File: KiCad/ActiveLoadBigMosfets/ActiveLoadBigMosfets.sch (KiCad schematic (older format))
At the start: 106 parts

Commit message: More PCB work
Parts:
- removed C? (x3): 10u/X7R/100V, symbol Device:C
- removed C?: 10u, symbol Device:C
- removed J?: FanOut, symbol Connector_Generic:Conn_01x03
- removed Q?: IRLML2244, Package_TO_SOT_SMD:SOT-23, symbol Transistor_FET:IRLML5203
- removed SW?: Rotary_Encoder_Switch, symbol Device:Rotary_Encoder_Switch
- removed U? (x3): TLV2372, symbol Amplifier_Operational:TLV2372
- added C13: 63SXV33M, Capacitor_SMD:CP_Elec_8x11.9, symbol Device:CP
- added C14: 4u7/16V/85mR, Capacitor_SMD:C_0805_2012Metric, symbol Device:C
- added C15: 10n, Capacitor_SMD:C_0805_2012Metric, symbol Device:C
- added C22, C48: 6TPE150MF, Capacitor_Tantalum_SMD:CP_EIA-7343-31_Kemet-D, symbol Device:CP
- added C31, C33, C35: 10u, Capacitor_SMD:C_0805_2012Metric, symbol Device:C
- added C34, C36, C49: 100n, Capacitor_SMD:C_0805_2012Metric, symbol Device:C
- added C40, C41, C42, C43, C44: 1n, Capacitor_SMD:C_0805_2012Metric, symbol Device:C
- added C50: 10u/10V, Capacitor_SMD:C_0805_2012Metric, symbol Device:C
- added F1: 10A, JPFuses:Fuseholder5x20_horiz_open_inline_Type-I, symbol Device:Fuse
- added FL1, FL2: BNX025, Filter:Filter_Murata_BNX025, symbol Filter:BNX025
- added H1, H2, H3, H4: MountingHole, MountingHole:MountingHole_3.2mm_M3, symbol Mechanical:MountingHole
- added J6: FanOut, Connector:FanPinHeader_1x04_P2.54mm_Vertical, symbol Connector_Generic:Conn_01x04
- added J7: PowerInput2, JPConnectors:SolderingHoles-2_P6.00mm_D2.0mm, symbol Connector_Generic:Conn_01x02
- added J8: PowerInput3, JPConnectors:SolderingHoles-2_P6.00mm_D2.0mm, symbol Connector_Generic:Conn_01x02
- added J9: PowerInput4, JPConnectors:SolderingHoles-2_P6.00mm_D2.0mm, symbol Connector_Generic:Conn_01x02
- added Q1: IRLML2502, Package_TO_SOT_SMD:SOT-23, symbol Transistor_FET:IRLML2060
- added Q10, Q11, Q12, Q13, Q14: IXFK44N50P, Package_TO_SOT_THT:TO-264-3_Vertical, symbol Device:Q_NMOS_GDS
- added R13: 100k, Resistor_SMD:R_0805_2012Metric, symbol Device:R
- added R27, R28, R29, R30, R32, R39, R40, R41, R42, R44, R64, R65: 10k, Resistor_SMD:R_0805_2012Metric, symbol Device:R
- added R33, R34, R35, R36, R37: 15k, Resistor_SMD:R_0805_2012Metric, symbol Device:R
- added R45, R46, R49, R50, R55: 0R1, Resistor_SMD:R_2512_6332Metric, symbol Device:R
- added R53, R54, R56, R57, R61: 1k, Resistor_SMD:R_0805_2012Metric, symbol Device:R
- added R63: 20m, Resistor_SMD:R_2512_6332Metric, symbol Device:R
- added R66, R67, R68, R69: 10, Resistor_SMD:R_0805_2012Metric, symbol Device:R
- added R70: 5k, Resistor_SMD:R_0805_2012Metric, symbol Device:R
- added RV1: 5k, Potentiometer_SMD:Potentiometer_ACP_CA6-VSMD_Vertical, symbol Device:R_POT
- added SW1: Rotary_Encoder_Switch, Rotary_Encoder:RotaryEncoder_Alps_EC11E-Switch_Vertical_H20mm_CircularMountingHoles, symbol Device:Rotary_Encoder_Switch
- added SW2: SW_Push, Button_Switch_SMD:SW_SPST_EVQP0, symbol Switch:SW_Push
- added U5, U6, U7: TLV2374, Package_SO:SOIC-14_3.9x8.7mm_P1.27mm, symbol myLib:TLV2374
- C1, C10, C16, C17, C18, C19, C2, C20, C21, C23, C24, C25, C26, C3, C30, C32, C37, C38, C39, C4, C45, C46, C47, C5, C6, C7, C8, C9: renamed from C?; footprint (none) -> Capacitor_SMD:C_0805_2012Metric
- C11, C12: renamed from C?; footprint (none) -> Capacitor_Tantalum_SMD:CP_EIA-7343-31_Kemet-D
- C27, C28: renamed from C?; value 10u/16V/85mR -> 4u7/16V/85mR; footprint (none) -> Capacitor_SMD:C_0805_2012Metric
- C29: renamed from C?; footprint (none) -> Capacitor_SMD:CP_Elec_6.3x7.7
- D1, D2: renamed from D?; footprint (none) -> Diode_SMD:D_SMB
- D3: renamed from D?; footprint (none) -> Diode_SMD:D_MiniMELF
- D4: renamed from D?; footprint (none) -> LED_SMD:LED_0805_2012Metric
- J1: renamed from J?; footprint (none) -> Connector_FFC-FPC:TE_0-1734839-6_1x06-1MP_P0.5mm_Horizontal
- J2: renamed from J?; footprint (none) -> JPConnectors:SolderingHoles-2_P6.00mm_D2.0mm
- J3: renamed from J?; footprint (none) -> Connector_PinHeader_2.54mm:PinHeader_1x06_P2.54mm_Vertical
- J4: renamed from J?; footprint (none) -> JPConnectors:Hirose_FH12-50S-0.5SH_1x50-1MP_P0.50mm_Horizontal
- J5: renamed from J?; footprint (none) -> Connector_PinHeader_2.54mm:PinHeader_2x10_P2.54mm_Vertical_SMD
- L1: renamed from L?; footprint (none) -> Inductor_SMD:L_0805_2012Metric
- L2: renamed from L?; footprint (none) -> JPInductors:L_Wuerth_WE-HCF
- L3: renamed from L?; value L -> 7447714330; footprint (none) -> Inductor_SMD:L_Wuerth_WE-PDF
- Q9: renamed from Q?; footprint (none) -> Package_TO_SOT_THT:TO-264-3_Vertical
- R1: renamed from R?; value R -> 20m; footprint (none) -> Resistor_SMD:R_2512_6332Metric
- R10, R12, R15, R16, R17, R18, R19, R2, R20, R21, R22, R24, R26, R38, R47, R48, R51, R52, R58, R59, R60, R62, R7, R8: renamed from R?; footprint (none) -> Resistor_SMD:R_0805_2012Metric
- R11: renamed from R?; value 133k -> 30k; footprint (none) -> Resistor_SMD:R_0805_2012Metric
- R14: renamed from R?; value 10k2 -> 15k4; footprint (none) -> Resistor_SMD:R_0805_2012Metric
- R23: renamed from R?; value 86k6 -> 100k; footprint (none) -> Resistor_SMD:R_0805_2012Metric
- R25: renamed from R?; value 10k -> 11k; footprint (none) -> Resistor_SMD:R_0805_2012Metric
- R3, R6: renamed from R?; footprint (none) -> Jumper:SolderJumper-2_P1.3mm_Bridged_RoundedPad1.0x1.5mm
- R31: renamed from R?; value 10k -> 15k; footprint (none) -> Resistor_SMD:R_0805_2012Metric
- R4, R5: renamed from R?; footprint (none) -> Jumper:SolderJumper-2_P1.3mm_Open_RoundedPad1.0x1.5mm
- R43: renamed from R?; footprint (none) -> Resistor_SMD:R_2512_6332Metric
- R9: renamed from R?; value 44k2 -> 68k; footprint (none) -> Resistor_SMD:R_0805_2012Metric
- U1: renamed from U?; footprint (none) -> Package_SO:SOIC-8-1EP_3.9x4.9mm_P1.27mm_EP2.41x3.3mm_ThermalVias
- U2: renamed from U?; footprint (none) -> Package_TO_SOT_SMD:SOT-223-3_TabPin2
- U4: renamed from U?; value LM2735XMF -> LM2735YMF
- U8: renamed from U?; footprint (none) -> Package_TO_SOT_THT:TO-220-5_Vertical
- Y1: renamed from Y?; footprint (none) -> Crystal:Crystal_SMD_5032-2Pin_5.0x3.2mm
- gave numbers to parts that had none: 9
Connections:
- net GNDPWR is gone; now on net GND: D1.2 (A), J2.1 (Pin_1), R43.2
- net +12V: now also C31.1, C33.1, C34.1, C35.1, C36.1, FL2.2 (CB), R70.1, U5.4 (V+), U6.4 (V+), U7.4 (V+); no longer C26.1, C27.1, C28.1, C29.1, D2.1 (K), R23.2
- net +3V3: now also C22.1, C49.1, R64.1, R66.2, R67.2, R68.2, R69.2; no longer R2.2
- net +4V: now also C48.1, C50.1, FL1.2 (CB); no longer C10.1, C11.1, C12.1, L2.2, R9.1
- net DisplayLEDCtrl: now also Q1.1 (G)
- net Enc_A: now also U3.22 (PA6); no longer U3.58 (PB6)
- net Enc_B: now also U3.23 (PA7); no longer U3.59 (PB7)
- net Enc_Switch: now also U3.41 (PA8); no longer U3.61 (PB8)
- net FanPWD: now also U3.21 (PA5), J6.4 (Pin_4); no longer Q8.1 (G), U3.22 (PA6)
- net FanSensor: now also U3.27 (PB1), J6.3 (Pin_3); no longer U3.23 (PA7)
- net GND: now also U1.7 (GND), U1.9 (PowerPAD), C13.2, FL1.3 (PSG), J7.1 (Pin_1), J8.1 (Pin_1), J9.1 (Pin_1), R13.2, R45.2, R46.2, R49.2, R50.2, R55.2; no longer C1.2, C17.2, C18.2, C19.2, C2.2, C20.2, C21.2, C23.2, C24.2, C25.1, C27.2, C28.2, C29.2, C3.2, C30.2, C32.2, C37.2, C38.2, C4.2, C45.2, C46.2, C47.2, C5.2, C6.2, C7.1, D3.2 (A), D4.1 (K), J1.6 (Pin_6), J3.3 (Pin_3), J4.1 (Pin_1), J4.11 (Pin_11), J4.12 (Pin_12), J4.13 (Pin_13), J4.14 (Pin_14), J4.34 (Pin_34), J4.43 (Pin_43), J4.48 (Pin_48), J4.49 (Pin_49), J4.50 (Pin_50), J4.8 (Pin_8), J4.9 (Pin_9), J5.10 (Pin_10), J5.12 (Pin_12), J5.14 (Pin_14), J5.16 (Pin_16), J5.18 (Pin_18), J5.20 (Pin_20), J5.4 (Pin_4), J5.6 (Pin_6), J5.8 (Pin_8), Q4.2 (S), Q5.2 (S), Q6.2 (S), Q7.2 (S), R11.2, R16.2, R17.2, R18.2, R19.2, R21.1, R25.1, R48.2, R5.2, R6.2, U2.2 (GND), U3.12 (VSSA), U3.18 (VSS), U3.31 (VSS), U3.47 (VSS), U3.60 (BOOT0), U3.63 (VSS), U4.2 (GND), U8.3 (GND), U9.1 (A1), U9.2 (A0), U9.7 (GND)
- net LCD_D_C: now also U3.59 (PB7)
- net LCD_RDX: now also U3.57 (PB5)
- net LCD_RESET: now also U3.50 (PA15)
- net LCD_SELECT: now also U3.61 (PB8)
- net LCD_WRX: now also U3.58 (PB6)
- net LED: now also U3.33 (PB12); no longer U3.50 (PA15)
- net LoadLevel: now also RV1.2, U5.10 (+), U5.5 (+), U6.10 (+), U6.5 (+), U7.10 (+), U7.5 (+)
- net PowerIn+: now also F1.1, R63.2; no longer J2.2 (Pin_2)
- net PowerIn-: now also U1.2 (Vin), U1.3 (EN), C13.1, Q10.2 (D), Q11.2 (D), Q12.2 (D), Q13.2 (D), Q14.2 (D), R63.1
- net at C39.2, Q9.1 (G): now also U5.7
- net at C39.1, R26.2: now also U5.6 (-)
- net at R38.2: now also U5.3 (+)
- net at R31.1, R48.1: now also U5.2 (-)
- net at R26.1, R31.2: now also U5.1
- net at D3.1 (K), Q8.2 (S): now also J6.2 (Pin_2)
- net at U1.1 (Boot): now also C8.2
- net at U1.4 (RT_SYNC): now also R11.1
- net at U1.5 (FB): now also C10.2, R14.1, R9.2
- net at U1.6 (SS): now also C16.1
- net at U1.8 (SW): now also C8.1, D1.1 (K), L2.2
- net Switch: now reaches U3.42 (PA9)
- net Switch: now also C15.1, R65.1
- net FanPower: now reaches U3.45 (PA12)
- net FanPower: now also Q8.1 (G)
- net GNDD: now reaches R20.1, R22.1
- net GNDD: now also C1.2, C17.2, C18.2, C19.2, C2.2, C20.2, C21.2, C23.2, C24.2, C25.1, C27.2, C28.2, C29.2, C3.2, C30.2, C37.2, C38.2, C4.2, C45.2, C46.2, C47.2, C5.2, C6.2, C7.1, D4.1 (K), J1.6 (Pin_6), J3.3 (Pin_3), J4.11 (Pin_11), J4.12 (Pin_12), J4.13 (Pin_13), J4.14 (Pin_14), J4.34 (Pin_34), J4.43 (Pin_43), J4.48 (Pin_48), J4.49 (Pin_49), J4.50 (Pin_50), J4.8 (Pin_8), J4.9 (Pin_9), J5.10 (Pin_10), J5.12 (Pin_12), J5.14 (Pin_14), J5.16 (Pin_16), J5.18 (Pin_18), J5.20 (Pin_20), J5.4 (Pin_4), J5.6 (Pin_6), J5.8 (Pin_8), Q4.2 (S), Q5.2 (S), Q6.2 (S), Q7.2 (S), R16.2, R17.2, R18.2, R19.2, R2.2, R21.1, R25.1, R5.2, R6.2, U2.2 (GND), U3.12 (VSSA), U3.18 (VSS), U3.31 (VSS), U3.47 (VSS), U3.60 (BOOT0), U3.63 (VSS), U4.2 (GND), U8.3 (GND), U9.1 (A1), U9.2 (A0), U9.7 (GND), C14.2, C15.2, C22.2, C48.2, C49.2, C50.2, FL1.4 (CG), FL2.3 (PSG), Q1.2 (S), RV1.3, SW1.C, SW1.S2, SW2.1
- net at R52.2, R58.1: now also SW1.B
- net at R51.2, R62.1: now also SW1.A
- net at R47.2, R59.2: now also SW1.S1
- new net: F1.2, J2.2 (Pin_2), J7.2 (Pin_2), J8.2 (Pin_2), J9.2 (Pin_2)
- new net: C14.1, C26.1, C27.1, C28.1, C29.1, D2.1 (K), FL2.1 (B), R23.2
- new net: R11.2, R13.1
- new net: C10.1, C11.1, C12.1, FL1.1 (B), L2.1, R9.1
- new net: J4.1 (Pin_1), Q1.3 (D)
- new net: J4.2 (Pin_2), R66.1
- new net: J4.3 (Pin_3), R67.1
- new net: J4.4 (Pin_4), R68.1
- new net: J4.5 (Pin_5), R69.1
- new net: R70.2, RV1.1
- new net: C40.2, Q10.1 (G), U5.8
- new net: C40.1, R27.2, U5.9 (-)
- new net: R39.2, U5.12 (+)
- new net: R33.1, R53.1, U5.13 (-)
- new net: R27.1, R33.2, U5.14
- new net: Q10.3 (S), R39.1, R45.1
- new net: C41.2, Q11.1 (G), U6.7
- new net: Q11.3 (S), R40.1, R46.1
- new net: R34.1, R54.1, U6.2 (-)
- new net: R40.2, U6.3 (+)
- new net: R28.1, R34.2, U6.1
- new net: C41.1, R28.2, U6.6 (-)
- new net: C42.2, Q12.1 (G), U6.8
- new net: C42.1, R29.2, U6.9 (-)
- new net: R41.2, U6.12 (+)
- new net: R35.1, R56.1, U6.13 (-)
- new net: R29.1, R35.2, U6.14
- new net: Q12.3 (S), R41.1, R49.1
- new net: C43.2, Q13.1 (G), U7.7
- new net: Q13.3 (S), R42.1, R50.1
- new net: R36.1, R57.1, U7.2 (-)
- new net: R42.2, U7.3 (+)
- new net: R30.1, R36.2, U7.1
- new net: C43.1, R30.2, U7.6 (-)
- new net: C44.2, Q14.1 (G), U7.8
- new net: C44.1, R32.2, U7.9 (-)
- new net: R44.2, U7.12 (+)
- new net: R37.1, R61.1, U7.13 (-)
- new net: R32.1, R37.2, U7.14
- new net: Q14.3 (S), R44.1, R55.1
- new net: R64.2, R65.2, SW2.2
- new net GNDA: C31.2, C32.2, C33.2, C34.2, C35.2, C36.2, D3.2 (A), FL2.4 (CG), J6.1 (Pin_1), R48.2, R53.2, R54.2, R56.2, R57.2, R61.2, U5.11 (V-), U6.11 (V-), U7.11 (V-)
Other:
- note added: "G=15"
- note added: "Rthjc=0.2Ohm\nRthcs=1Ohm\nRthsa=0.5Ohm\nRth=1.7Ohm\n(125-40)/1.7=50W\n\nRth=0.25+0+0.5=0.75 Ohm\n85/0.75=114W"
- note added: "Vo=12.665V"
- note added: "Vo=4.062V"
- note added: "https://webench.ti.com/power-designer/switching-regulator/customize/8?AppType=None&Flavor=NA&O1I=1.5&O1V=4&Topology=BUCK&VinMax=30.00&VinMin=5&VoltageOption=NA&base_pn=LMR14020S&flavor=NA&lang_chosen=en_US&op_TA=30&optfactor=3&origin=pf_panel\nhttps://webench.ti.com/power-designer/switching-regulator/customize/7?AppType=None&Flavor=None&O1I=0.4&O1V=12&Topology=Boost&VinMax=4&VinMin=4&VoltageOptio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"
- note removed: "G=10"
- note removed: "Rthjc=0.25Ohm\nRthcs=1Ohm\nRthsa=0.5Ohm\nRth=1.75Ohm\n\n(125-40)/2.25=48W"
- note removed: "https://webench.ti.com/power-designer/switching-regulator/customize/8?AppType=None&Flavor=NA&O1I=1.5&O1V=4&Topology=BUCK&VinMax=30.00&VinMin=5&VoltageOption=NA&base_pn=LMR14020S&flavor=NA&lang_chosen=en_US&op_TA=30&optfactor=3&origin=pf_panel"
- moved on the sheet: C1, C10, C11, C12, C16, C19, C20, C21, C23, C24, C25, C26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

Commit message: More pcb work
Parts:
- added J10: I2C, Connector_PinHeader_2.54mm:PinHeader_1x04_P2.54mm_Vertical, symbol Connector_Generic:Conn_01x04
- C2, C20, C21, C23, C24, C25, C3, C32, C34, C36, C37, C38, C4, C49, C5, C7, C8, C9: footprint Capacitor_SMD:C_0805_2012Metric -> Capacitor_SMD:C_0603_1608Metric
- FL1, FL2: footprint Filter:Filter_Murata_BNX025 -> JPInductors:Filter_Murata_BNX025
- L3: footprint Inductor_SMD:L_Wuerth_WE-PDF -> JPInductors:L_Wuerth_WE-PDF_Handsoldering
- R1, R43, R45, R46, R49, R50, R55, R63: footprint Resistor_SMD:R_2512_6332Metric -> Resistor_SMD:R_2512_6332Metric_Pad1.52x3.35mm_HandSolder
- R10, R12, R20, R21, R22, R24, R26, R27, R28, R29, R30, R32, R38, R39, R40, R41, R42, R44, R47, R51, R52, R58, R59, R60, R62, R64, R65: footprint Resistor_SMD:R_0805_2012Metric -> Resistor_SMD:R_0603_1608Metric
- U4: footprint Package_TO_SOT_SMD:SOT-23-5 -> Package_TO_SOT_SMD:SOT-23-5_HandSoldering
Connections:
- net +3V3: now also J10.1 (Pin_1)
- net GNDD: now also J10.2 (Pin_2)
- net SCL: now also J10.3 (Pin_3)
- net SDA: now also J10.4 (Pin_4)

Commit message: PCB work
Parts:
- J4: footprint JPConnectors:Hirose_FH12-50S-0.5SH_1x50-1MP_P0.50mm_Horizontal -> JPConnectors:Molex-50S-0.5SH_1x50-P0.50mm_Horizontal
- SW2: footprint Button_Switch_SMD:SW_SPST_EVQP0 -> Button_Switch_SMD:SW_SPST_B3S-1000
- U8: footprint Package_TO_SOT_THT:TO-220-5_Vertical -> Connector_PinHeader_2.54mm:PinHeader_1x05_P2.54mm_Vertical
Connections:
- net LCD_RESET: now also U3.49 (PA14); no longer U3.50 (PA15)
- net SCL: now also U8.4 (SCLK); no longer U8.2 (SDA)
- net SDA: now also U8.2 (SDA); no longer U8.4 (SCLK)
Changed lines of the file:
@@
 F 0 "U8" H 4823 8038 40  0000 R CNN
 F 1 "TC74" H 4823 7962 40  0000 R CNN
-F 2 "Package_TO_SOT_THT:TO-220-5_Vertical" H 4950 8000 60  0001 C CNN
+F 2 "Connector_PinHeader_2.54mm:PinHeader_1x05_P2.54mm_Vertical" H 4950 8000 60  0001 C CNN
 F 3 "" H 4950 8000 60  0000 C CNN
 	1    4950 8000
@@
 	1    0    0    -1
 $EndComp
-Text GLabel 5400 7950 2    50   Input ~ 0
+Text GLabel 5400 8050 2    50   Input ~ 0
 SCL
 Text GLabel 6250 2300 2    50   Input ~ 0
 SCL
-Text GLabel 5400 8050 2    50   Input ~ 0
+Text GLabel 5400 7950 2    50   Input ~ 0
 SDA
 Wire Wire Line
@@
 F 0 "J4" H 12850 4067 50  0000 C CNN
 F 1 "RVT28AETNWC00" H 12850 3976 50  0000 C CNN
-F 2 "JPConnectors:Hirose_FH12-50S-0.5SH_1x50-1MP_P0.50mm_Horizontal" H 12800 2650 50  0001 C CNN
+F 2 "JPConnectors:Molex-50S-0.5SH_1x50-P0.50mm_Horizontal" H 12800 2650 50  0001 C CNN
 F 3 "~" H 12800 2650 50  0001 C CNN
 	1    12800 2650
@@
 Wire Wire Line
 	1000 6000 1000 6150
-Text Label 9850 4300 0    50   ~ 0
+Text Label 9850 4200 0    50   ~ 0
 LCD_RESET
 Wire Wire Line
@@
 F 0 "SW2" H 1700 12285 50  0000 C CNN
 F 1 "SW_Push" H 1700 12194 50  0000 C CNN
-F 2 "Button_Switch_SMD:SW_SPST_EVQP0" H 1700 12200 50  0001 C CNN
+F 2 "Button_Switch_SMD:SW_SPST_B3S-1000" H 1700 12200 50  0001 C CNN
 F 3 "~" H 1700 12200 50  0001 C CNN
 	1    1700 12000

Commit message: Latest PCB changes. STM32 Project
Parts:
- removed Y1: Crystal, Crystal:Crystal_SMD_5032-2Pin_5.0x3.2mm, symbol Device:Crystal
- added Q15, Q16: IRLML2244, Package_TO_SOT_SMD:SOT-23, symbol Transistor_FET:IRLML5203
- added Q17: IRLML2502, Package_TO_SOT_SMD:SOT-23, symbol Transistor_FET:IRLML2060
- added R71, R72: 100k, Resistor_SMD:R_0805_2012Metric, symbol Device:R
- added TP1, TP10, TP11, TP12, TP2, TP3, TP4, TP5, TP6, TP7, TP8, TP9: TestPoint, TestPoint:TestPoint_THTPad_1.5x1.5mm_Drill0.7mm, symbol Connector:TestPoint
- added Y1: 16MHz, Crystal:Crystal_SMD_Abracon_ABM3B-4Pin_5.0x3.2mm, symbol Device:Crystal_GND24
- R60: value 10k -> 4k7; footprint Resistor_SMD:R_0603_1608Metric -> Resistor_SMD:R_0805_2012Metric
- R7, R8: value 2k2 -> 4k7
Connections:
- net +12V: now also Q15.2 (S), Q16.2 (S), R71.2, R72.2, TP6.1; no longer C31.1, C32.1, C33.1, C34.1, C35.1, C36.1, Q8.3 (D), U5.4 (V+), U6.4 (V+), U7.4 (V+)
- net +3V3: now also TP11.1
- net +4V: now also TP2.1
- net DisplayLEDCtrl: now also U3.45 (PA12); no longer U3.46 (PA13)
- net FanSensor: now also U3.62 (PB9); no longer U3.27 (PB1)
- net GND: now also TP3.1
- net GNDA: now also C33.1, Q8.2 (S), Q17.2 (S), TP8.1; no longer C33.2
- net GNDD: now also TP10.1, TP12.1, TP4.1, TP7.1, Y1.2, Y1.4
- net LCD_RESET: now also U3.50 (PA15); no longer U3.49 (PA14)
- net LoadLevel: now also TP9.1
- net SWCLK: now also U3.49 (PA14); no longer U3.35 (PB14)
- net SWDIO: now also U3.46 (PA13); no longer U3.34 (PB13)
- net at C14.1, C26.1, C27.1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: now also TP5.1
- net at C10.1, C11.1, C12.1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: now also TP1.1
- net at C17.1, U3.5 (PH0): now also Y1.1
- net at D3.1 (K), J6.2 (Pin_2): now also Q15.3 (D); no longer Q8.2 (S)
- net at C18.1, R15.2: now also Y1.3
- net FanPWD renamed FanPWM
- net FanPower renamed FanPowerCtrl
- net FanPowerCtrl: now also U3.35 (PB14); no longer U3.45 (PA12)
- new net: Q15.1 (G), Q8.3 (D), R71.1
- new net: Q16.1 (G), Q17.3 (D), R72.1
- new net LoadOpAmpsPower: C31.1, C32.1, C33.2, C34.1, C35.1, C36.1, Q16.3 (D), U5.4 (V+), U6.4 (V+), U7.4 (V+)
- new net LoadOpAmpsPowerCtrl: Q17.1 (G), U3.34 (PB13)
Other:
- note added: "1 ADC step\non MTU = 1/4096 * 3.3V = 0.8mV\non power shunt = 0.8mV / 15 = 0.054mV\nwhich corresponds to 0.054mV / 100mOhm = 0.54mA\n"
- note added: "G=15\nVaplified=15*200mV=3V"
- note added: "R=100mOhm\nImax = 2A\nVmax = 200mV\nPmax = 400mW"
- note removed: "R=100mOhm\nImax = 2A\nVmax = 200mA\nPmax = 400mW"
- moved on the sheet: C31, C32, C33, C34, C35, C36, C39, C40, C41, C42, C43, C44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

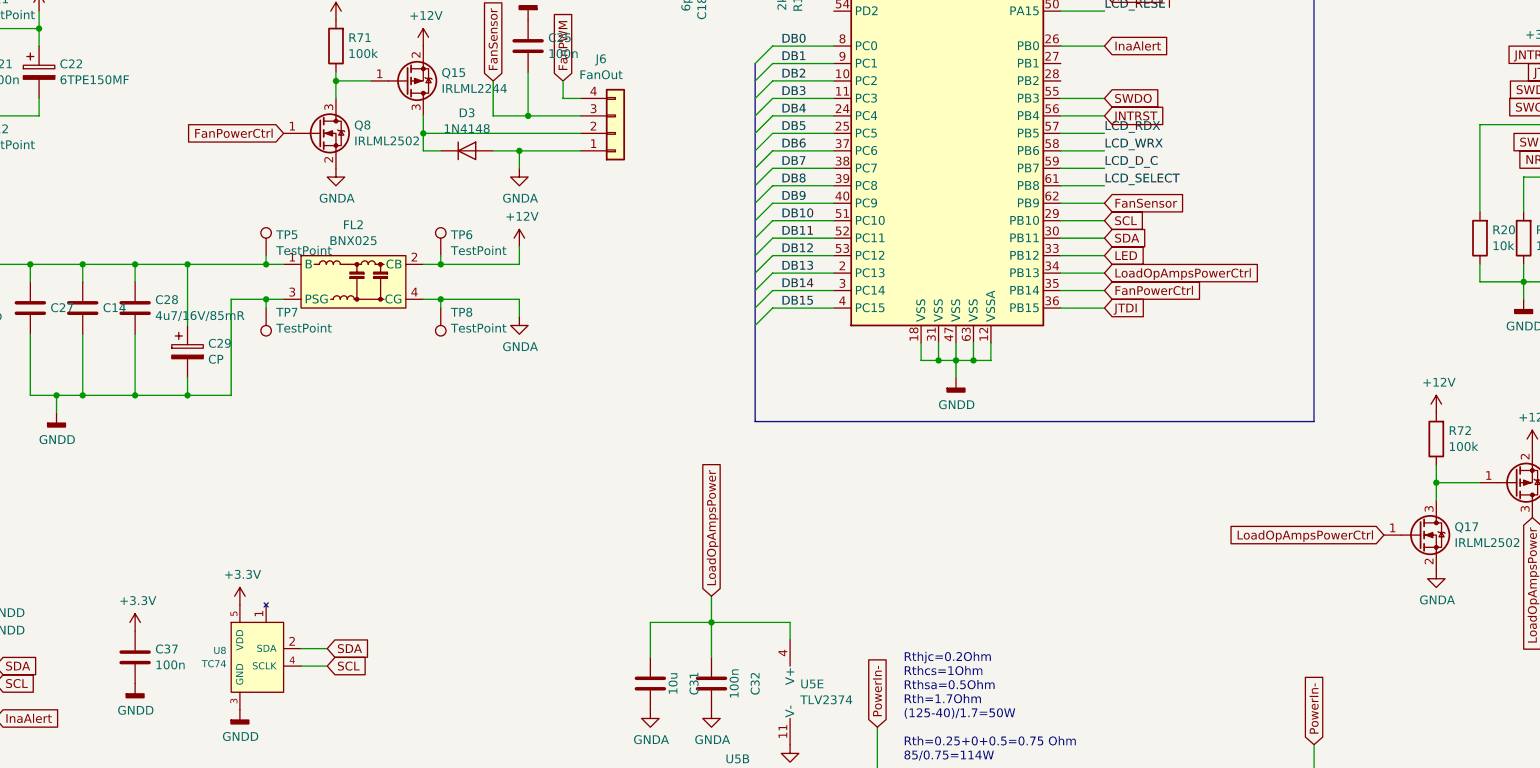
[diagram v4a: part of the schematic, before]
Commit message: Fan controller added
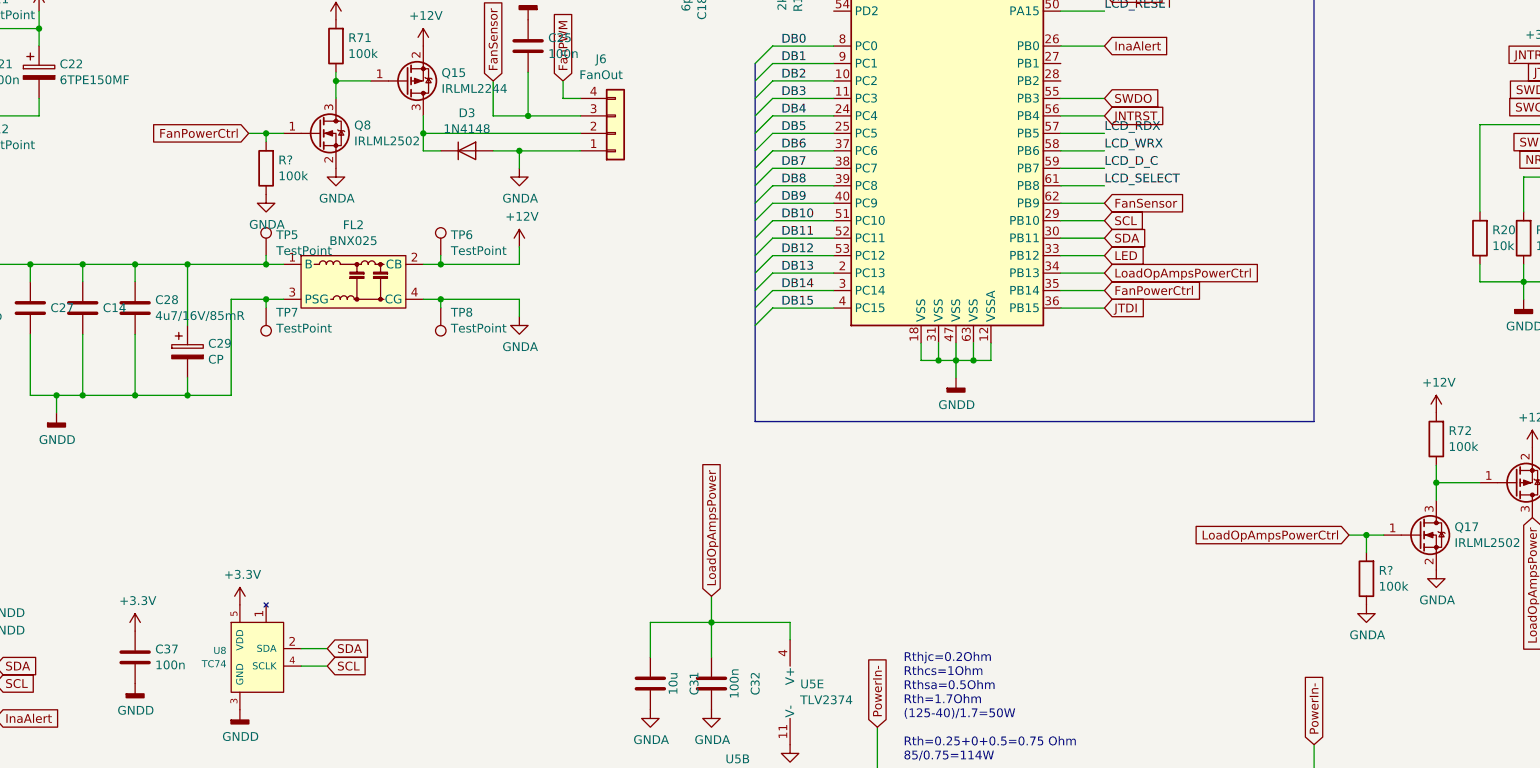
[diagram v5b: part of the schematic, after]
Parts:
- added R? (x2): 100k, Resistor_SMD:R_0805_2012Metric, symbol Device:R
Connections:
- net FanPowerCtrl: now also R?.2
- net GNDA: now also R?.1, R?.1
- net LoadOpAmpsPowerCtrl: now also R?.2
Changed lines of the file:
@@
 $EndComp
 Connection ~ 4000 5750
-Text GLabel 5150 5000 0    50   Input ~ 0
+Text GLabel 4950 5000 0    50   Input ~ 0
 FanPowerCtrl
 Text GLabel 9850 3300 2    50   Input ~ 0
@@
 Wire Wire Line
 	11750 7000 11750 7100
-Text GLabel 11450 7300 0    50   Input ~ 0
+Text GLabel 11250 7300 0    50   Input ~ 0
 LoadOpAmpsPowerCtrl
 $Comp
@@
 Wire Wire Line
 	9600 5400 9850 5400
+$Comp
+L Device:R R?
+U 1 1 5EC4AE22
+P 11350 7550
+F 0 "R?" H 11280 7504 50  0000 R CNN
+F 1 "100k" H 11280 7595 50  0000 R CNN
+F 2 "Resistor_SMD:R_0805_2012Metric" V 11280 7550 50  0001 C CNN
+F 3 "~" H 11350 7550 50  0001 C CNN
+	1    11350 7550
+	-1   0    0    1
+$EndComp
+Wire Wire Line
+	11250 7300 11350 7300
+Wire Wire Line
+	11350 7400 11350 7300
+Connection ~ 11350 7300
+Wire Wire Line
+	11350 7300 11450 7300
+$Comp
+L power:GNDA #PWR?
+U 1 1 5ED5E84F
+P 11350 7700
+F 0 "#PWR?" H 11350 7450 50  0001 C CNN
+F 1 "GNDA" H 11355 7527 50  0000 C CNN
+F 2 "" H 11350 7700 50  0001 C CNN
+F 3 "" H 11350 7700 50  0001 C CNN
+	1    11350 7700
+	1    0    0    -1
+$EndComp
+$Comp
+L Device:R R?
+U 1 1 5ED5ED19
+P 5050 5200
+F 0 "R?" H 4980 5154 50  0000 R CNN
+F 1 "100k" H 4980 5245 50  0000 R CNN
+F 2 "Resistor_SMD:R_0805_2012Metric" V 4980 5200 50  0001 C CNN
+F 3 "~" H 5050 5200 50  0001 C CNN
+	1    5050 5200
+	-1   0    0    1
+$EndComp
+$Comp
+L power:GNDA #PWR?
+U 1 1 5ED5F4B1
+P 5050 5350
+F 0 "#PWR?" H 5050 5100 50  0001 C CNN
+F 1 "GNDA" H 5055 5177 50  0000 C CNN
+F 2 "" H 5050 5350 50  0001 C CNN
+F 3 "" H 5050 5350 50  0001 C CNN
+	1    5050 5350
+	1    0    0    -1
+$EndComp
+Wire Wire Line
+	4950 5000 5050 5000
+Wire Wire Line
+	5050 5050 5050 5000
 Wire Bus Line
 	17050 4300 17050 4650
@@
 Wire Bus Line
 	7850 4600 7850 6650
+Connection ~ 5050 5000
+Wire Wire Line
+	5050 5000 5150 5000
 $EndSCHEMATC

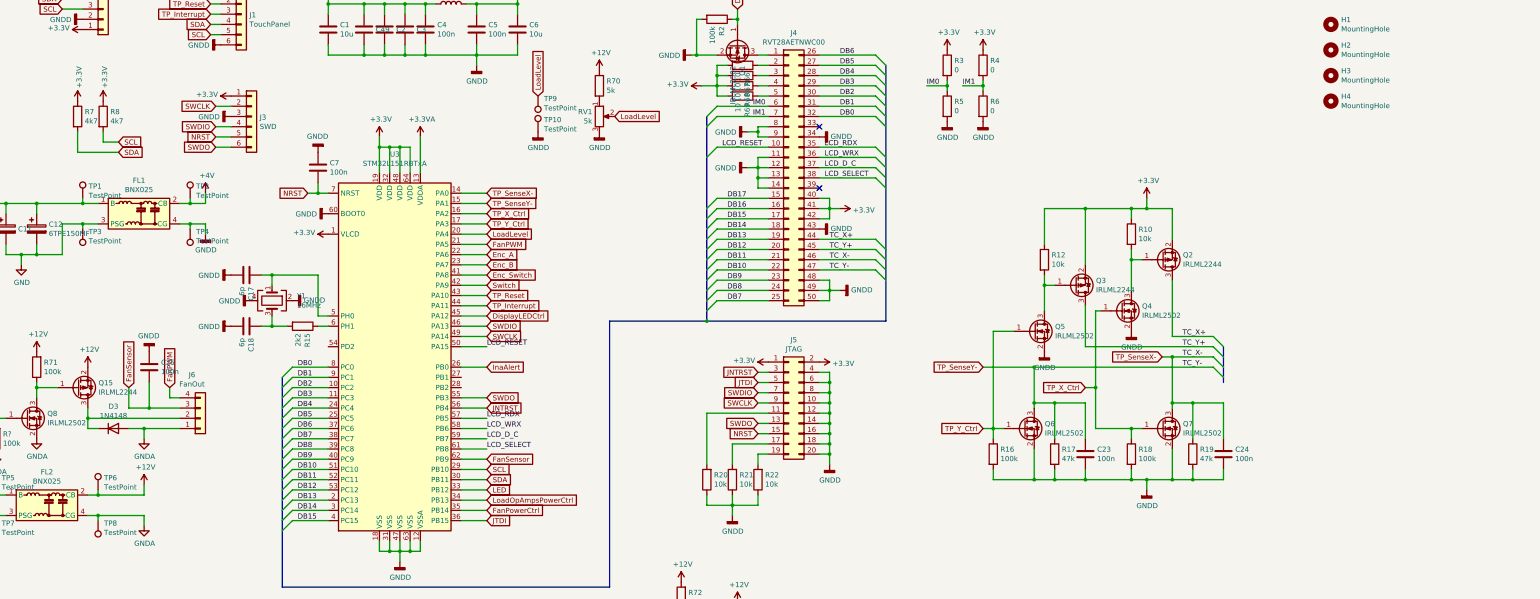
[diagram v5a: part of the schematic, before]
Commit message: Fan RPM measurement added
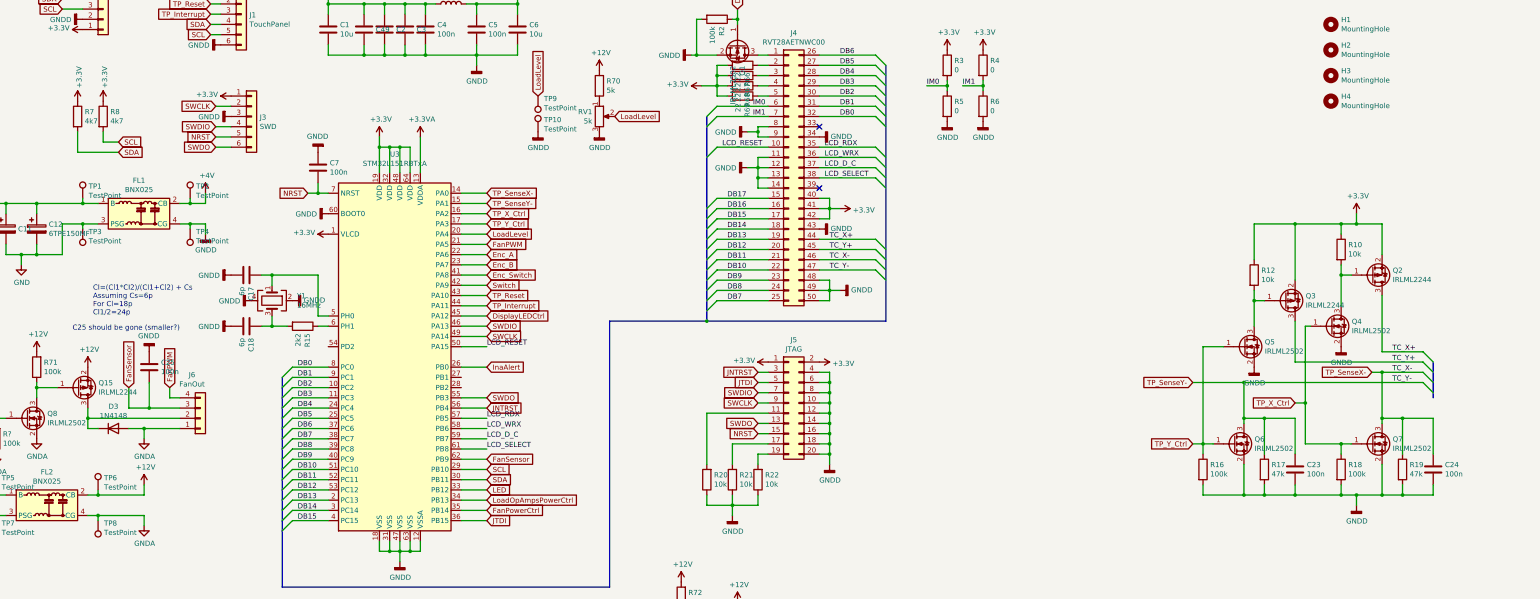
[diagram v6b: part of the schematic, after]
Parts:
- R66, R67, R68, R69: value 10 -> 22
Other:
- note added: "C25 should be gone (smaller?)"
- note added: "Cl=(Cl1*Cl2)/(Cl1+Cl2) + Cs\nAssuming Cs=6p\nFor Cl=18p\nCl1/2=24p"
- moved on the sheet: C23, C24, Q2, Q3, Q4, Q5, Q6, Q7, R10, R12, R16, R17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
